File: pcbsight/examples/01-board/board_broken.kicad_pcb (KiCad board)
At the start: 3 parts

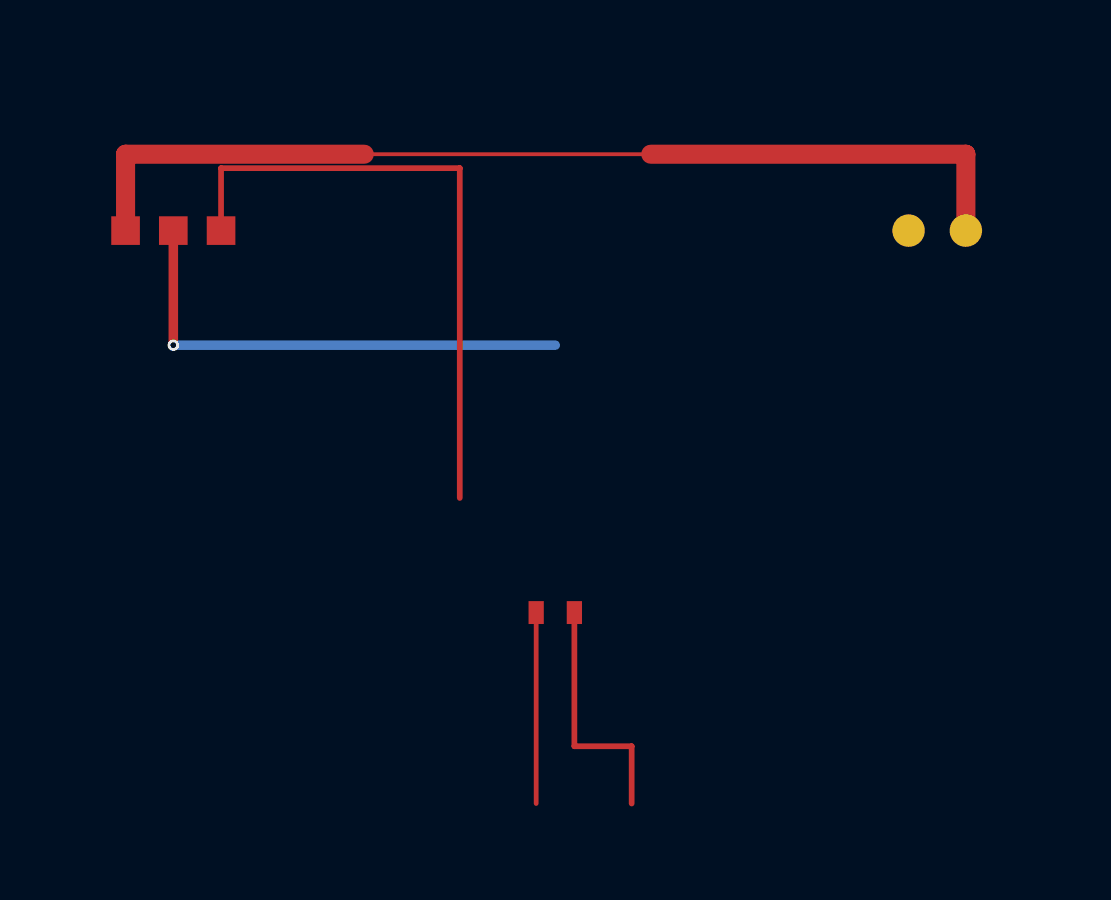
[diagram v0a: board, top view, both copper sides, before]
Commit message: pcbsight: the render now looks like a board, not loose wires
The user was right - a PCB render must read as a PCB. The board model
and renderer were rebuilt around that:

board.py now parses what makes a board a board:
- Footprint entities: reference (U1, J1...), value, world placement,
  and a BODY outline composed from F.SilkS / F.Fab / courtyard graphics
  - or inferred from the pad bbox when a footprint ships no graphics, so
  a component is never invisible (flagged body_inferred).
- Edge.Cuts -> the substrate outline; board.outline_rect() falls back to
  the copper bbox + 2 mm when a file has none.
- pad rotation carried through.

render.py is a board-shop drawing: soldermask-green substrate sized to
Edge.Cuts, a faint 10 mm grid, gold F.Cu / dim B.Cu copper, tin pads
with drills, vias, white silkscreen component outlines with their
reference AND value, and findings circled in red at their coordinates.
Title bar states size / component count / net count.

The examples' generator gained edge_rect + silk bodies + values (shared
helper examples/_kicad.py for the richer boards to come); 01-board
regenerated - it now shows a 54x43 substrate with U1 "AP2112", J1
"PWR", J2 "USB" as named, outlined parts. Two parser tests added.

Co-Authored-By: Claude Opus 4.8 <noreply@anthropic.com>
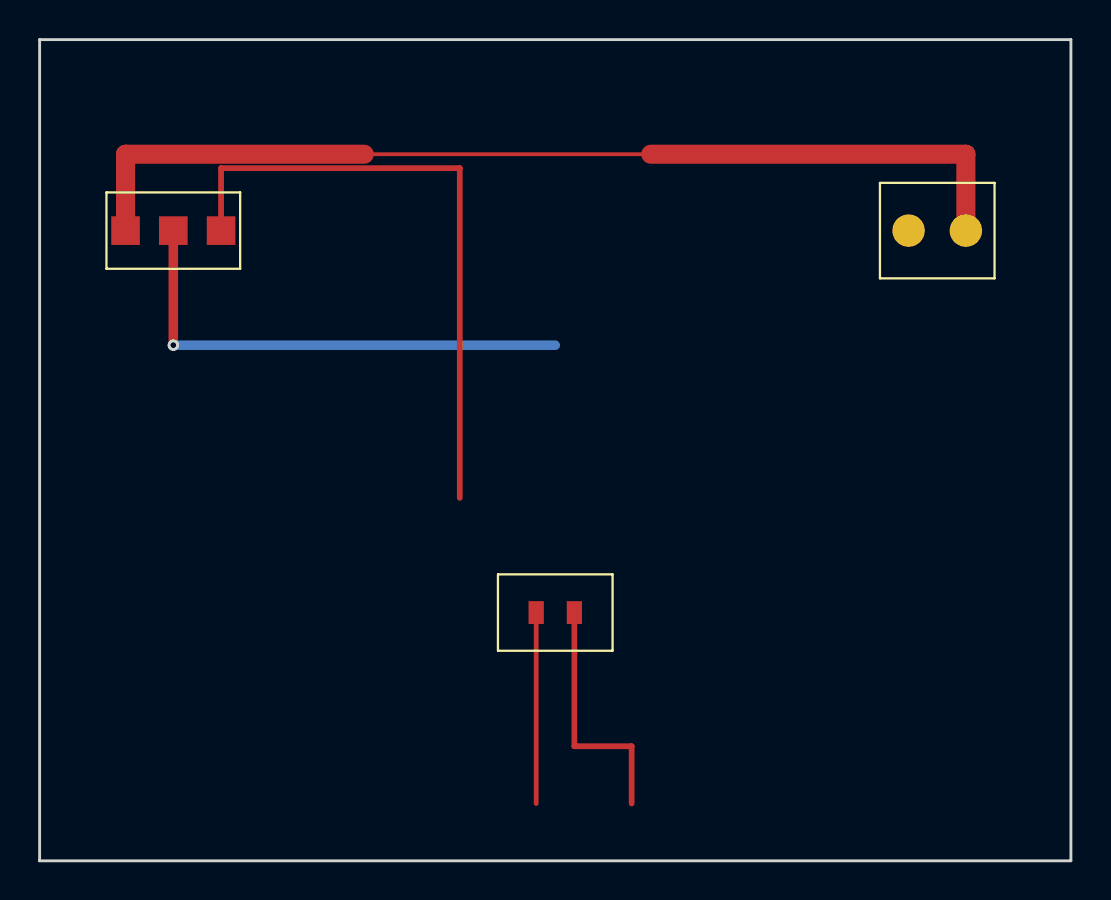
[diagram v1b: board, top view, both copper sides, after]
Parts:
- J1: value (none) -> PWR
- J2: value (none) -> USB
- U1: value (none) -> AP2112
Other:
- board outline added: 54 x 43 mm
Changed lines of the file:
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@@
   (net 4 "USB_N")
   (net 5 "SIG")
-  (footprint "generic:U1" (at 20 20 0)
-    (property "Reference" "U1" (at 0 -2))
+  (gr_line (start 13 10) (end 67 10) (layer "Edge.Cuts") (width 0.15))
+  (gr_line (start 67 10) (end 67 53) (layer "Edge.Cuts") (width 0.15))
+  (gr_line (start 67 53) (end 13 53) (layer "Edge.Cuts") (width 0.15))
+  (gr_line (start 13 53) (end 13 10) (layer "Edge.Cuts") (width 0.15))
+  (footprint "generic:U1" (at 20 20 0) (layer "F.Cu")
+    (property "Reference" "U1" (at 0 -3.2))
+    (property "Value" "AP2112" (at 0 3.2))
+    (fp_line (start -3.5 -2.0) (end 3.5 -2.0) (layer "F.SilkS") (width 0.12))
+    (fp_line (start 3.5 -2.0) (end 3.5 2.0) (layer "F.SilkS") (width 0.12))
+    (fp_line (start 3.5 2.0) (end -3.5 2.0) (layer "F.SilkS") (width 0.12))
+    (fp_line (start -3.5 2.0) (end -3.5 -2.0) (layer "F.SilkS") (width 0.12))
     (pad "1" smd rect (at -2.5 0) (size 1.5 1.5) (layers "F.Cu" "F.Mask") (net 1 "+5V"))
     (pad "2" smd rect (at 0 0) (size 1.5 1.5) (layers "F.Cu" "F.Mask") (net 2 "GND"))
     (pad "3" smd rect (at 2.5 0) (size 1.5 1.5) (layers "F.Cu" "F.Mask") (net 5 "SIG"))
   )
-  (footprint "generic:J1" (at 60 20 180)
-    (property "Reference" "J1" (at 0 -2))
+  (footprint "generic:J1" (at 60 20 180) (layer "F.Cu")
+    (property "Reference" "J1" (at 0 -3.7))
+    (property "Value" "PWR" (at 0 3.7))
+    (fp_line (start -3.0 -2.5) (end 3.0 -2.5) (layer "F.SilkS") (width 0.12))
+    (fp_line (start 3.0 -2.5) (end 3.0 2.5) (layer "F.SilkS") (width 0.12))
+    (fp_line (start 3.0 2.5) (end -3.0 2.5) (layer "F.SilkS") (width 0.12))
+    (fp_line (start -3.0 2.5) (end -3.0 -2.5) (layer "F.SilkS") (width 0.12))
     (pad "1" thru_hole circle (at -1.5 0) (size 1.7 1.7) (layers "*.Cu" "*.Mask") (net 1 "+5V"))
     (pad "2" thru_hole circle (at 1.5 0) (size 1.7 1.7) (layers "*.Cu" "*.Mask") (net 2 "GND"))
   )
-  (footprint "generic:J2" (at 40 40 0)
-    (property "Reference" "J2" (at 0 -2))
+  (footprint "generic:J2" (at 40 40 0) (layer "F.Cu")
+    (property "Reference" "J2" (at 0 -3.2))
+    (property "Value" "USB" (at 0 3.2))
+    (fp_line (start -3.0 -2.0) (end 3.0 -2.0) (layer "F.SilkS") (width 0.12))
+    (fp_line (start 3.0 -2.0) (end 3.0 2.0) (layer "F.SilkS") (width 0.12))
+    (fp_line (start 3.0 2.0) (end -3.0 2.0) (layer "F.SilkS") (width 0.12))
+    (fp_line (start -3.0 2.0) (end -3.0 -2.0) (layer "F.SilkS") (width 0.12))
     (pad "1" smd rect (at -1.0 0) (size 0.8 1.2) (layers "F.Cu" "F.Mask") (net 3 "USB_P"))
     (pad "2" smd rect (at 1.0 0) (size 0.8 1.2) (layers "F.Cu" "F.Mask") (net 4 "USB_N"))
